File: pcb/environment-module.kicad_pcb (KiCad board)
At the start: 4 copper layers, 50 x 25 mm, 112 parts, among them J1 AVR-UPDI-6, U1 ATtiny1616-MNR, U2 PCA9545APW, U3 AHT20-F, U4 LTR-303ALS-01, U5 SGP40-D-R4

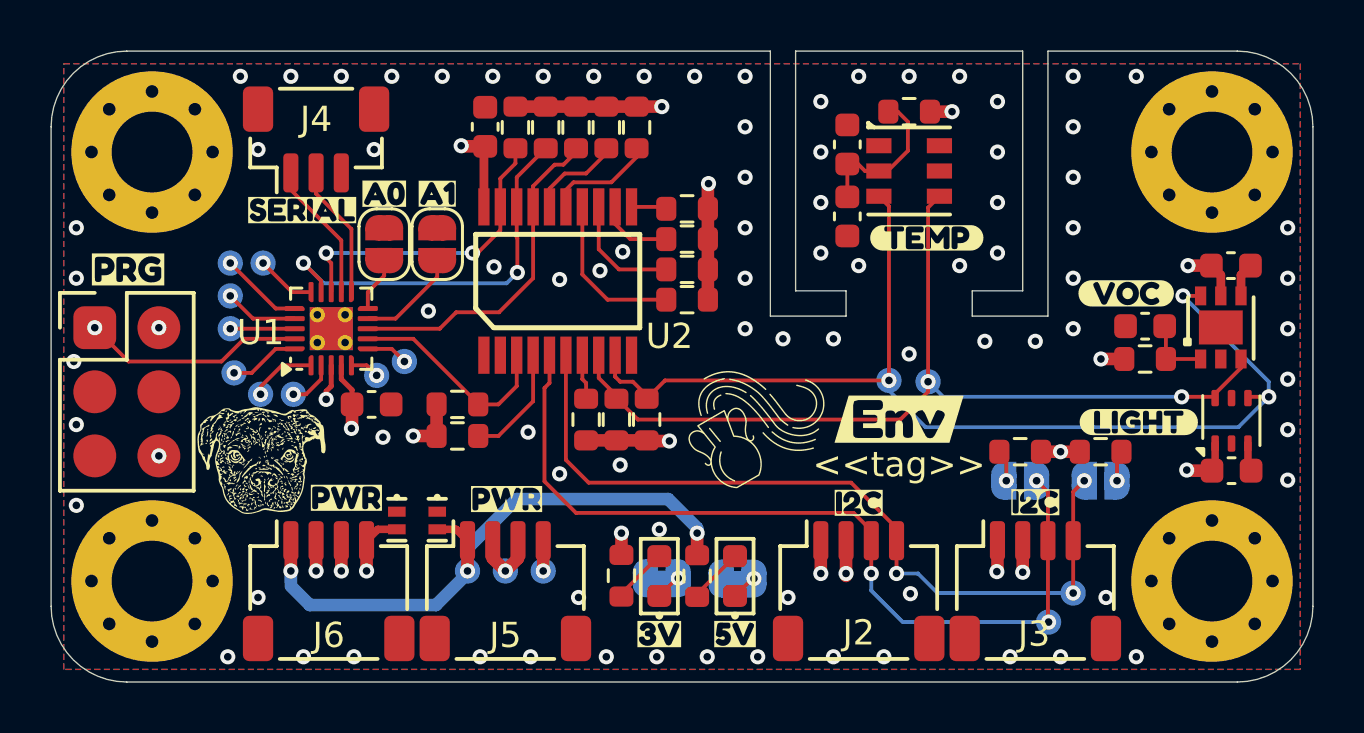
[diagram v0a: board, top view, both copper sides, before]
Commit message: Redesign with cutouts for sensors
Removed power connectors since 5V is not needed
Added cutout for VOC sensor
Rerouted sensor section
Rescaled logos and fixed silkscreen
Changed to blue LED for power indicator
Updated requirements and renders
Changed all 0.1uF caps to small symbol
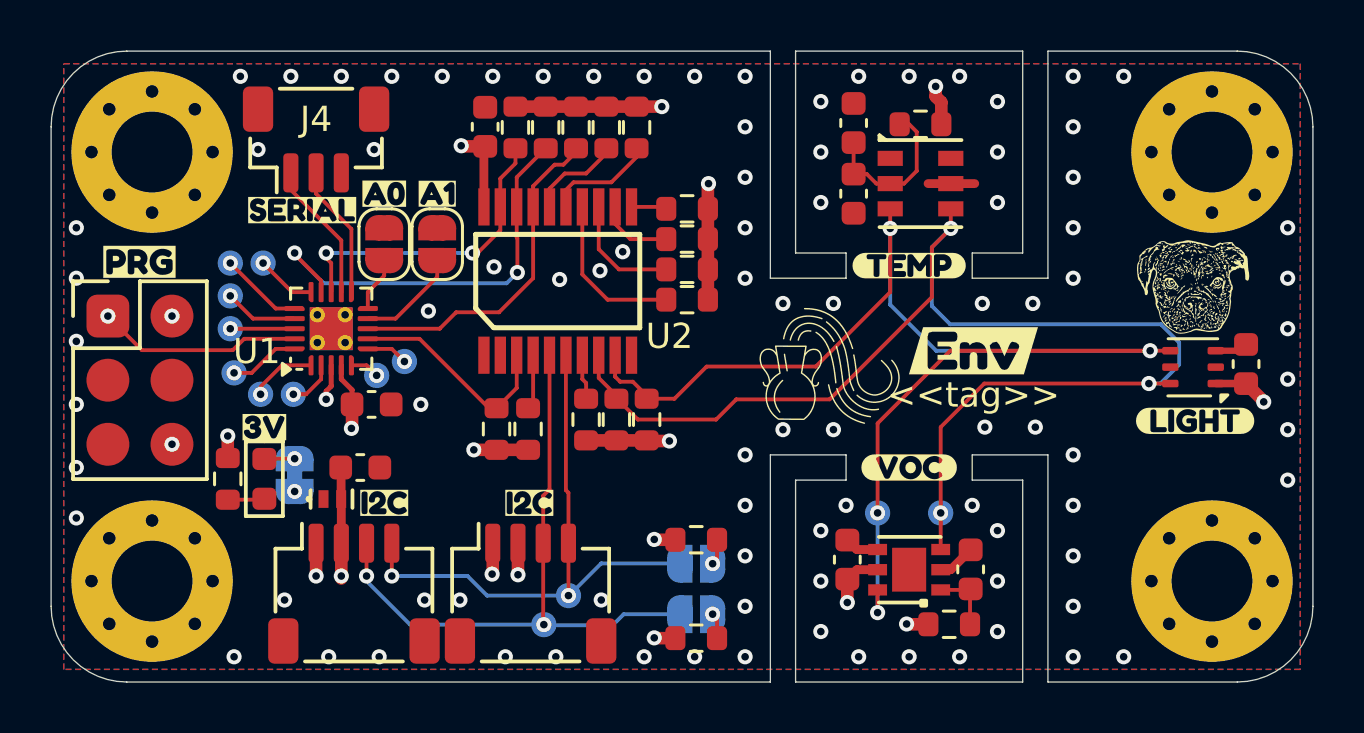
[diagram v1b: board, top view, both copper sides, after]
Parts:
- removed D3, D4: Orange, CRGM Passive:LED_0603_1608Metric
- removed J5, J6: ~, CRGM Connector:JST_SH_SM04B-SRSS-TB_1x04-1MP_P1.00mm_Horizontal
- removed JP5: ~, CRGM Connector:SolderJumper-2_P1.3mm_Bridged_RoundedPad1.0x1.5mm
- removed R15: 4.7K, CRGM Passive:R_0603_1608Metric
- removed TP15: ~, CRGM Mechanical:TestPoint_Pad_D1.0mm
- removed kibuzzard-68C1F3DD (x2): G***, kibuzzard-68C1F3DD
- removed kibuzzard-68FC4C50: G***, kibuzzard-68FC4C50
- removed kibuzzard-6902BBC2: G***, kibuzzard-6902BBC2
- removed kibuzzard-6908DD8D: G***, kibuzzard-6908DD8D
- removed kibuzzard-690A7D9E: G***, kibuzzard-690A7D9E
- removed kibuzzard-690D67FA: G***, kibuzzard-690D67FA
- removed kibuzzard-695039AD: G***, kibuzzard-695039AD
- added C8: 10uF, CRGM Passive:C_0603_1608Metric, F.Cu at (62.2, 141.5)
- added kibuzzard-69571EBA: G***, kibuzzard-69571EBA, B.Cu at (62.9, 136.2)
- added kibuzzard-69571EDB: G***, kibuzzard-69571EDB, B.Cu at (56.8, 139.1)
- added kibuzzard-69571F0B: G***, kibuzzard-69571F0B, B.Cu at (85.2, 141.0)
- D1: value PESD5V5C1BL -> Blue; footprint CRGM Passive:DFN1006-2 -> CRGM Passive:LED_0603_1608Metric
- LOGO5: footprint CRGM Logos:Roxy 5mm -> CRGM Logos:Roxy 4mm
- moved LOGO5 37.6 mm to (95.3, 134.4)
- moved kibuzzard-691D233B 25.6 mm to (94.2, 135.2)
- moved kibuzzard-68F7F6E1 20.1 mm to (73.7, 145.3)
- moved kibuzzard-690D683A 20.1 mm to (66.8, 147.8)
- moved kibuzzard-68FAFCDC 20.1 mm to (69.0, 142.9)
- moved J2 20.0 mm to (62.0, 146.5)
- moved J3 20.0 mm to (69.0, 146.5)
- moved TP13 20.0 mm to (70.5, 146.6)
- moved TP14 20.0 mm to (69.5, 147.7)
- moved kibuzzard-690D6835 19.9 mm to (69.0, 144.7)
- moved C5 19.2 mm to (81.5, 145.2), turned to 90 degrees
- moved kibuzzard-68FAFCDC 18.8 mm to (63.2, 142.9)
- moved kibuzzard-68FC4C43 18.8 mm to (53.3, 133.9), turned to 135 degrees
- moved TP16 17.8 mm to (54.8, 135.5), turned to 90 degrees
- moved kibuzzard-690A7D98 17.7 mm to (58.5, 139.9)
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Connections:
- D1 pad 1: GND -> Net-(D1-K)
- D1 pad 2: +5V -> /Power/V3.3LED
- JP6 pad 2: Net-(D4-K) -> Net-(D1-K)
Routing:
- net +5V: track 24.4 -> 0.00 mm, vias 3 -> 0
- net /Peripherals/INT_SDA: track 36.3 -> 51.4 mm, vias 2 -> 3
- net /Peripherals/INT_SCL: track 42.8 -> 52.4 mm, vias 3 -> 4
- net EXT_SDA: track 34.7 -> 26.1 mm, vias 3 -> 2
- net EXT_SCL: track 32.2 -> 23.7 mm, vias 3 -> 2
- net Net-(U2-~{INT0}): track 4.57 -> 1.90 mm
- net /Power/V5LED: track 2.12 -> 0.00 mm
- net GND: track 11.5 -> 9.64 mm, vias 90 -> 96
- net Net-(D1-K): track 0.00 -> 1.19 mm, vias 0 -> 1
- net MCU_SCL: track 15.8 -> 16.9 mm
- net Net-(D4-K): track 1.04 -> 0.00 mm, vias 1 -> 0
- net Net-(D3-K): track 1.03 -> 0.00 mm, vias 1 -> 0
- net /Power/V3.3LED: track 2.12 -> 1.41 mm
- net /MCU/UPDI: track 8.85 -> 8.15 mm
- net +3.3V: track 36.6 -> 36.8 mm, vias 17 -> 16
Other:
- outline, holes or cut-outs redrawn

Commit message: Removed FNWW logo
Adjusted silkscreen on back
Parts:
- removed LOGO7: ~, CRGM Logos:FNWW Face 5mm
- moved kibuzzard-691D233B 6.90 mm to (87.6, 137.1)
- moved LOGO6 0.75 mm to (70.2, 137.7)
